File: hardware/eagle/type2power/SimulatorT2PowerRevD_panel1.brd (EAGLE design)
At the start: 99.1 x 99.1 mm, 49 parts

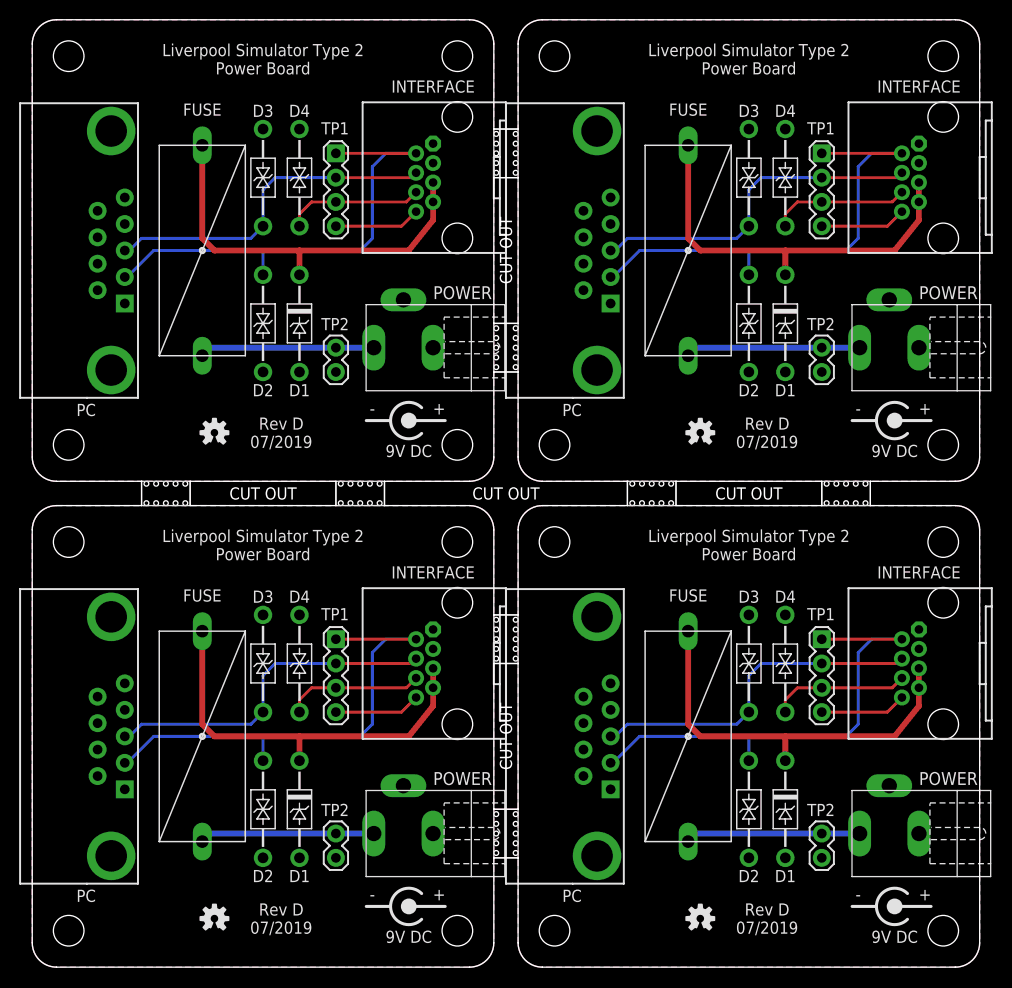
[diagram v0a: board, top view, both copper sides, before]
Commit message: Board Housekeeping
URL on silkscreens, caution messages, tidy up naming conventions.
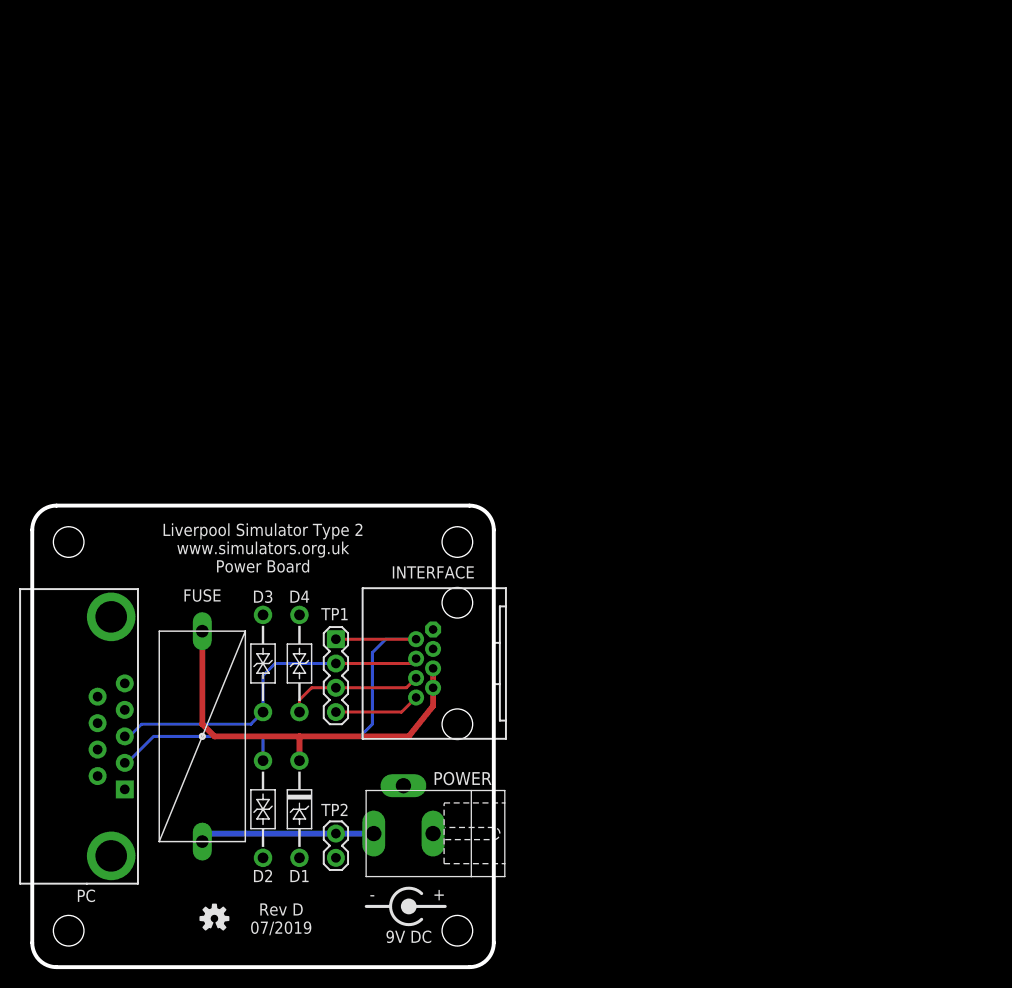
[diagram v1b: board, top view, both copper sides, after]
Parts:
- removed D1_1, D1_2, D1_3: SA12A, AIC_Custom:DO41_TVS_UNI
- removed D2_1, D2_2, D2_3, D3_1, D3_2, D3_3, D4_1, D4_2, D4_3: SA15CA, AIC_Custom:DO41_TVS_BI
- removed E$2: (no value), AIC_Custom:OUTLINE_PANEL_4_5MM
- removed FUSE_1, FUSE_2, FUSE_3: 800mA, AIC_Custom:MCOMP-FUSE-HOLDER-PCB
- removed INTERFACE_1, INTERFACE_2, INTERFACE_3: RJ45-RJHSE-X08090DEG, AIC_Custom:RJ45-RJHSE-5080
- removed LOGO1_1, LOGO1_2, LOGO1_3: OSHW-LOGOS, SparkFun-Aesthetics:OSHW-LOGO-S
- removed PC_1, PC_2, PC_3: (no value), AIC_Custom:MULTICOMP-DB9-FEMALE-PCB-90DEG
- removed POWER_1, POWER_2, POWER_3: 9V DC, AIC_Custom:CLIFF-FC681465P-DC-JACK
- removed TP1_1, TP1_2, TP1_3: (no value), SparkFun-Connectors:1X04
- removed TP2_1, TP2_2, TP2_3: (no value), SparkFun-Connectors:1X02
- removed U$1_1, U$1_2, U$1_3: (no value), AIC_Custom:CENTRE-POS-SILK
- added E$1: (no value), AIC_Custom:WARNING_TRIANGLE_TPLACE
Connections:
- removed net GND1: D1_1.ANODE, D2_1.A, D3_1.A, D4_1.A, INTERFACE_1.1, INTERFACE_1.3, PC_1.5, POWER_1.3, TP2_1.2
- removed net GND2: D1_2.ANODE, D2_2.A, D3_2.A, D4_2.A, INTERFACE_2.1, INTERFACE_2.3, PC_2.5, POWER_2.3, TP2_2.2
- removed net GND3: D1_3.ANODE, D2_3.A, D3_3.A, D4_3.A, INTERFACE_3.1, INTERFACE_3.3, PC_3.5, POWER_3.3, TP2_3.2
- removed net P81: INTERFACE_1.8, TP1_1.4
- removed net P82: INTERFACE_2.8, TP1_2.4
- removed net P83: INTERFACE_3.8, TP1_3.4
- removed net RXD1: D3_1.C, INTERFACE_1.4, PC_1.3, TP1_1.2
- removed net RXD2: D3_2.C, INTERFACE_2.4, PC_2.3, TP1_2.2
- removed net RXD3: D3_3.C, INTERFACE_3.4, PC_3.3, TP1_3.2
- removed net TX21: D4_1.C, INTERFACE_1.6, TP1_1.3
- removed net TX22: D4_2.C, INTERFACE_2.6, TP1_2.3
- removed net TX23: D4_3.C, INTERFACE_3.6, TP1_3.3
- removed net TXD1: D2_1.C, INTERFACE_1.2, PC_1.2, TP1_1.1
- removed net TXD2: D2_2.C, INTERFACE_2.2, PC_2.2, TP1_2.1
- removed net TXD3: D2_3.C, INTERFACE_3.2, PC_3.2, TP1_3.1
- removed net VIN1: FUSE_1.2, POWER_1.1, TP2_1.1
- removed net VIN21: D1_1.CATHODE, FUSE_1.1, INTERFACE_1.5, INTERFACE_1.7
- removed net VIN22: D1_2.CATHODE, FUSE_2.1, INTERFACE_2.5, INTERFACE_2.7
- removed net VIN23: D1_3.CATHODE, FUSE_3.1, INTERFACE_3.5, INTERFACE_3.7
- removed net VIN3: FUSE_2.2, POWER_2.1, TP2_2.1
- removed net VIN4: FUSE_3.2, POWER_3.1, TP2_3.1
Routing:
- net TXD3: track 51.1 -> 0.00 mm
- net TXD2: track 51.1 -> 0.00 mm
- net TXD1: track 51.1 -> 0.00 mm
- net VIN21: track 42.4 -> 0.00 mm
- net VIN23: track 42.4 -> 0.00 mm
- net VIN22: track 42.4 -> 0.00 mm
- net RXD3: track 36.1 -> 0.00 mm
- net RXD2: track 36.1 -> 0.00 mm
- net RXD1: track 36.1 -> 0.00 mm
- net VIN1: track 18.3 -> 0.00 mm
- net VIN4: track 18.3 -> 0.00 mm
- net VIN3: track 18.3 -> 0.00 mm
- net TX23: track 14.4 -> 0.00 mm
- net TX21: track 14.4 -> 0.00 mm
- net TX22: track 14.4 -> 0.00 mm
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- removed copper zone on layer 1, net GND1
- removed copper zone on layer 16, net GND1
- removed copper zone on layer 1, net GND2
- removed copper zone on layer 16, net GND2
- removed copper zone on layer 1, net GND3
- removed copper zone on layer 16, net GND3
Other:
- board size 99.1 x 99.1 mm -> 48.3 x 48.3 mm
- board text added: "Connect this board to Liverpool Simulator Type 2 or compatible equipment ONLY. Refer to documentation for details."
- board text added: "Liverpool Simulator Type 2 www.simulators.org.uk Power Board"
- board text removed: "Liverpool Simulator Type 2 Power Board"
